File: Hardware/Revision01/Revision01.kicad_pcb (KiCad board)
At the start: 4 copper layers, 100 x 119.8 mm, 63 parts, among them J1 Battery connector, J2 StrainConn, J3 StrainConn, J4 StrainConn, J5 StrainConn, J6 StrainConn, J7 StrainConn, J8 StrainConn, J9 StrainConn, Q3 NMOS, Q4 PMOS, Q6 PMOS, SW2 SW_SPST_LED, U10 NCP1117LPST50T3G, U11 LP5813BDRRR, U2 MRF89XAM9AT-I/RM, U3 NUCLEO-L476RG, U4 ICM-45605

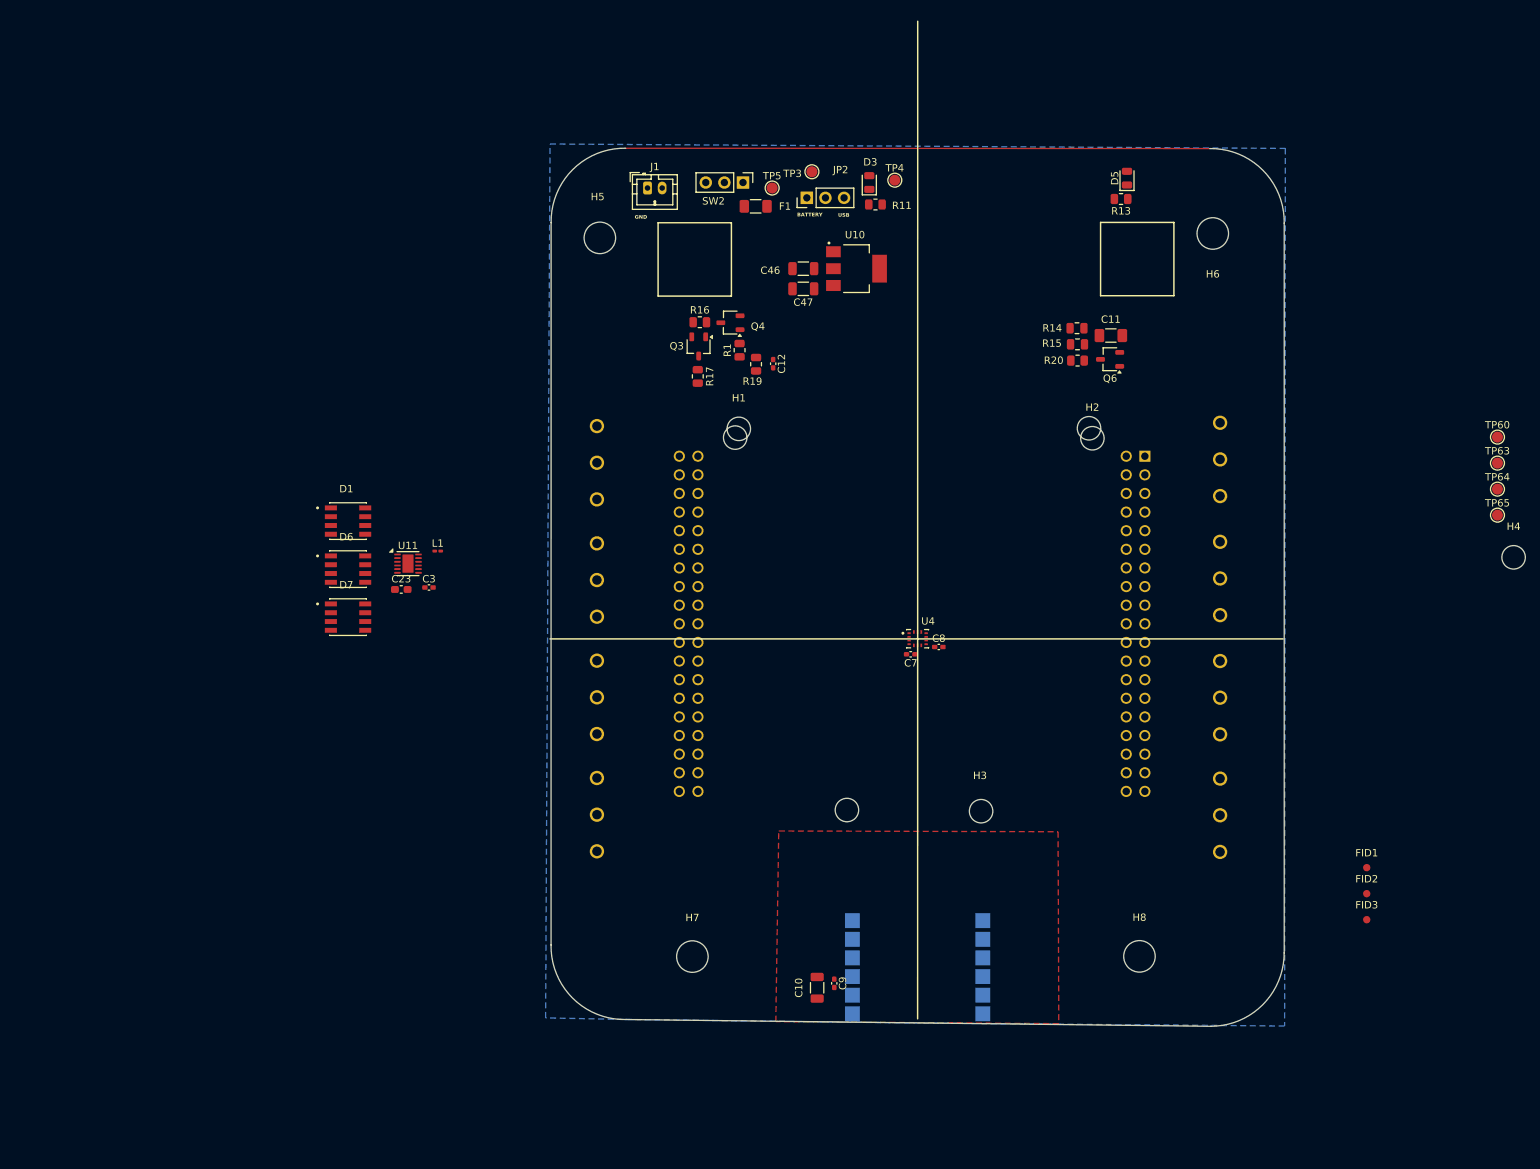
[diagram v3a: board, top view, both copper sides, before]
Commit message: I believe I have finished schematic
-Calculated RC circuit with cutoff at 10KHz for ADC
- Stimulated OP-AMP circuit with strainGauge
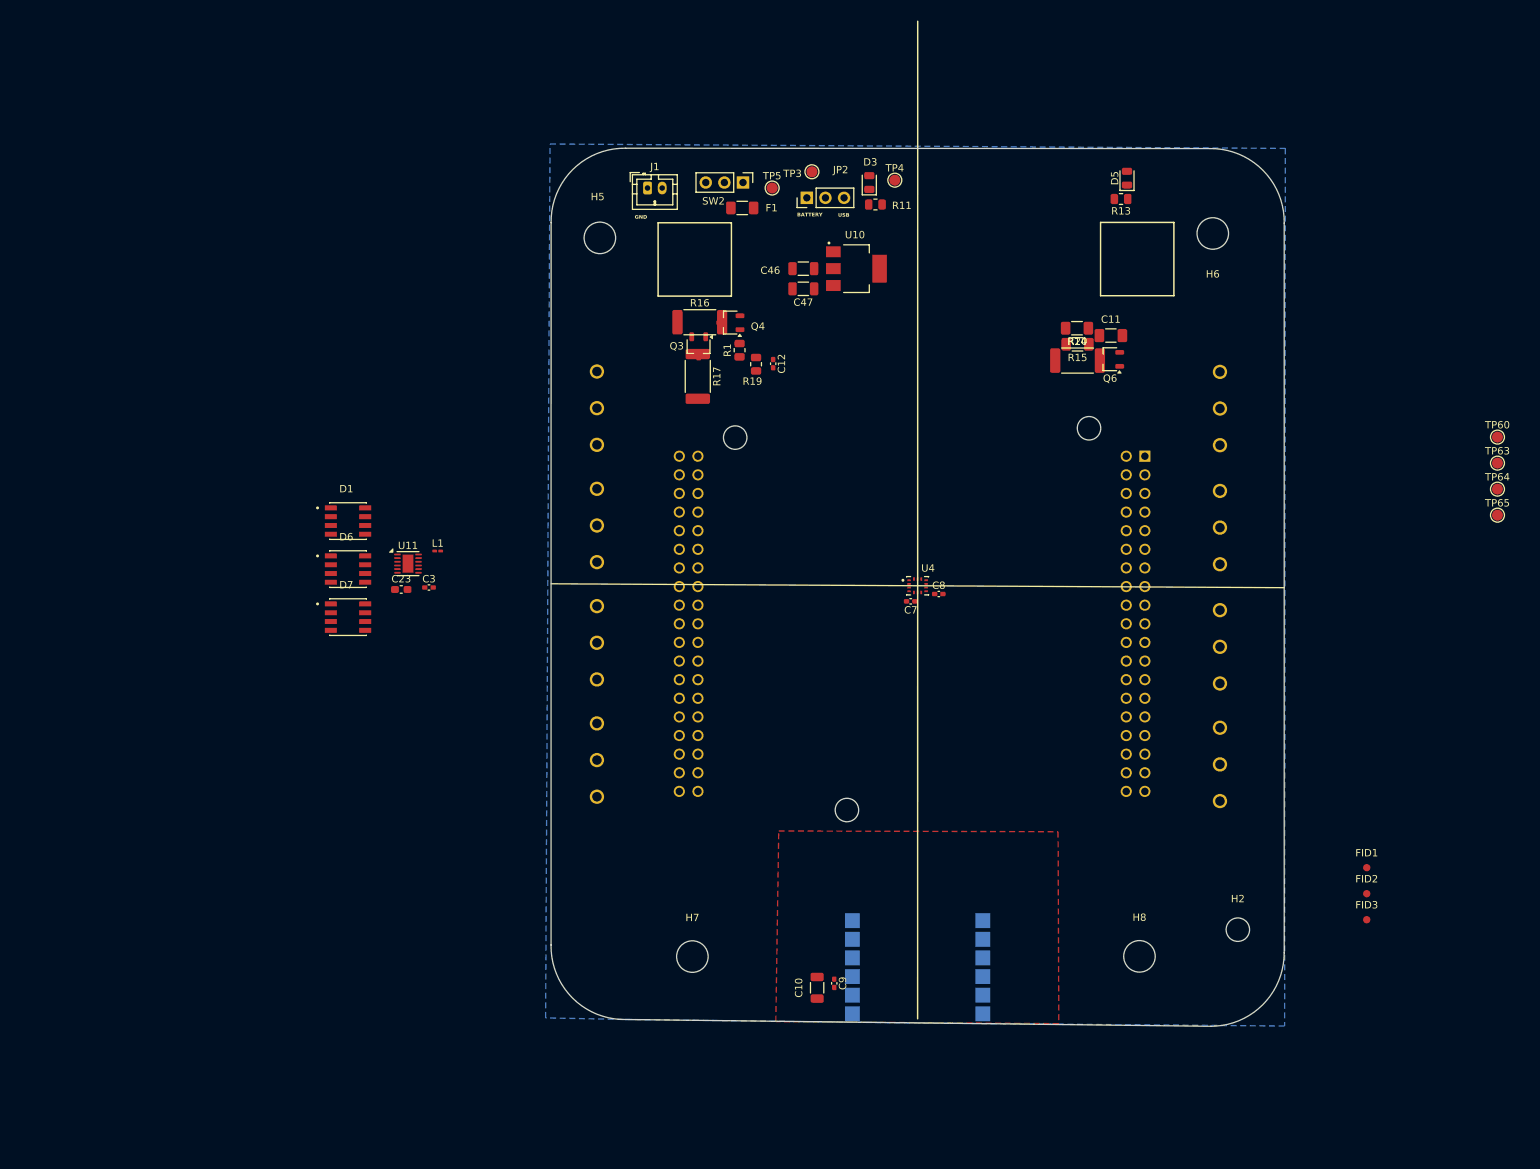
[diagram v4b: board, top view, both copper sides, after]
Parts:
- removed H1, H3, H4: MountingHole, MountingHole:MountingHole_3.2mm_M3
- R14, R15: footprint Capacitor_SMD:C_0805_2012Metric -> Resistor_SMD:R_1206_3216Metric_Pad1.30x1.75mm_HandSolder
- R16, R17, R20: value 10K +-5% -> 10K +-1%; footprint Resistor_SMD:R_0805_2012Metric -> Resistor_SMD:R_2512_6332Metric_Pad1.40x3.35mm_HandSolder
- moved H2 69.9 mm to (204.7, 139.5)
- moved J2 7.44 mm to (117.3, 116.4)
- moved J3 7.44 mm to (117.3, 100.4)
- moved J4 7.44 mm to (117.3, 84.4)
- moved J5 7.44 mm to (117.3, 68.4)
- moved C7 7.22 mm to (160.1, 94.8)
- moved C8 7.22 mm to (163.9, 93.8)
- moved U4 7.22 mm to (161.0, 92.6)
- moved J6 6.94 mm to (202.3, 117.0)
- moved J7 6.94 mm to (202.3, 84.7)
- moved J8 6.94 mm to (202.3, 68.5)
- moved J9 6.94 mm to (202.3, 101.0)
- moved F1 1.84 mm to (137.1, 41.1)
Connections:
- J2 pad 1: /Application/+StrainV -> GND
- J2 pad 3: GND -> /Application/+StrainV
- J3 pad 1: /Application/+StrainV -> GND
- J3 pad 3: GND -> /Application/+StrainV
- J4 pad 1: /Application/+StrainV -> GND
- J4 pad 3: GND -> /Application/+StrainV
- J5 pad 1: /Application/+StrainV -> GND
- J5 pad 3: GND -> /Application/+StrainV
- J6 pad 1: /Application/+StrainV -> GND
- J6 pad 3: GND -> /Application/+StrainV
- J7 pad 1: /Application/+StrainV -> GND
- J7 pad 3: GND -> /Application/+StrainV
- J8 pad 1: /Application/+StrainV -> GND
- J8 pad 3: GND -> /Application/+StrainV
- J9 pad 1: /Application/+StrainV -> GND
- J9 pad 3: GND -> /Application/+StrainV

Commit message: schematic wiring, and LT-SPICE simulations on strain gauge - Added buffer with offset at 1.66V to instrumentation amplifier to ensure -20-20mv range can be read - Added caps to Instrumentation Amplifier circuit - Stimulated straingauge->Amplifier->Adc with all components imported. Verified ADC can read between 0.3-3.0V - Created second draft bom, component cost at around 212$ - Changed many components to Automotive grade - Added breathingCUBE led driver to prototype my own project
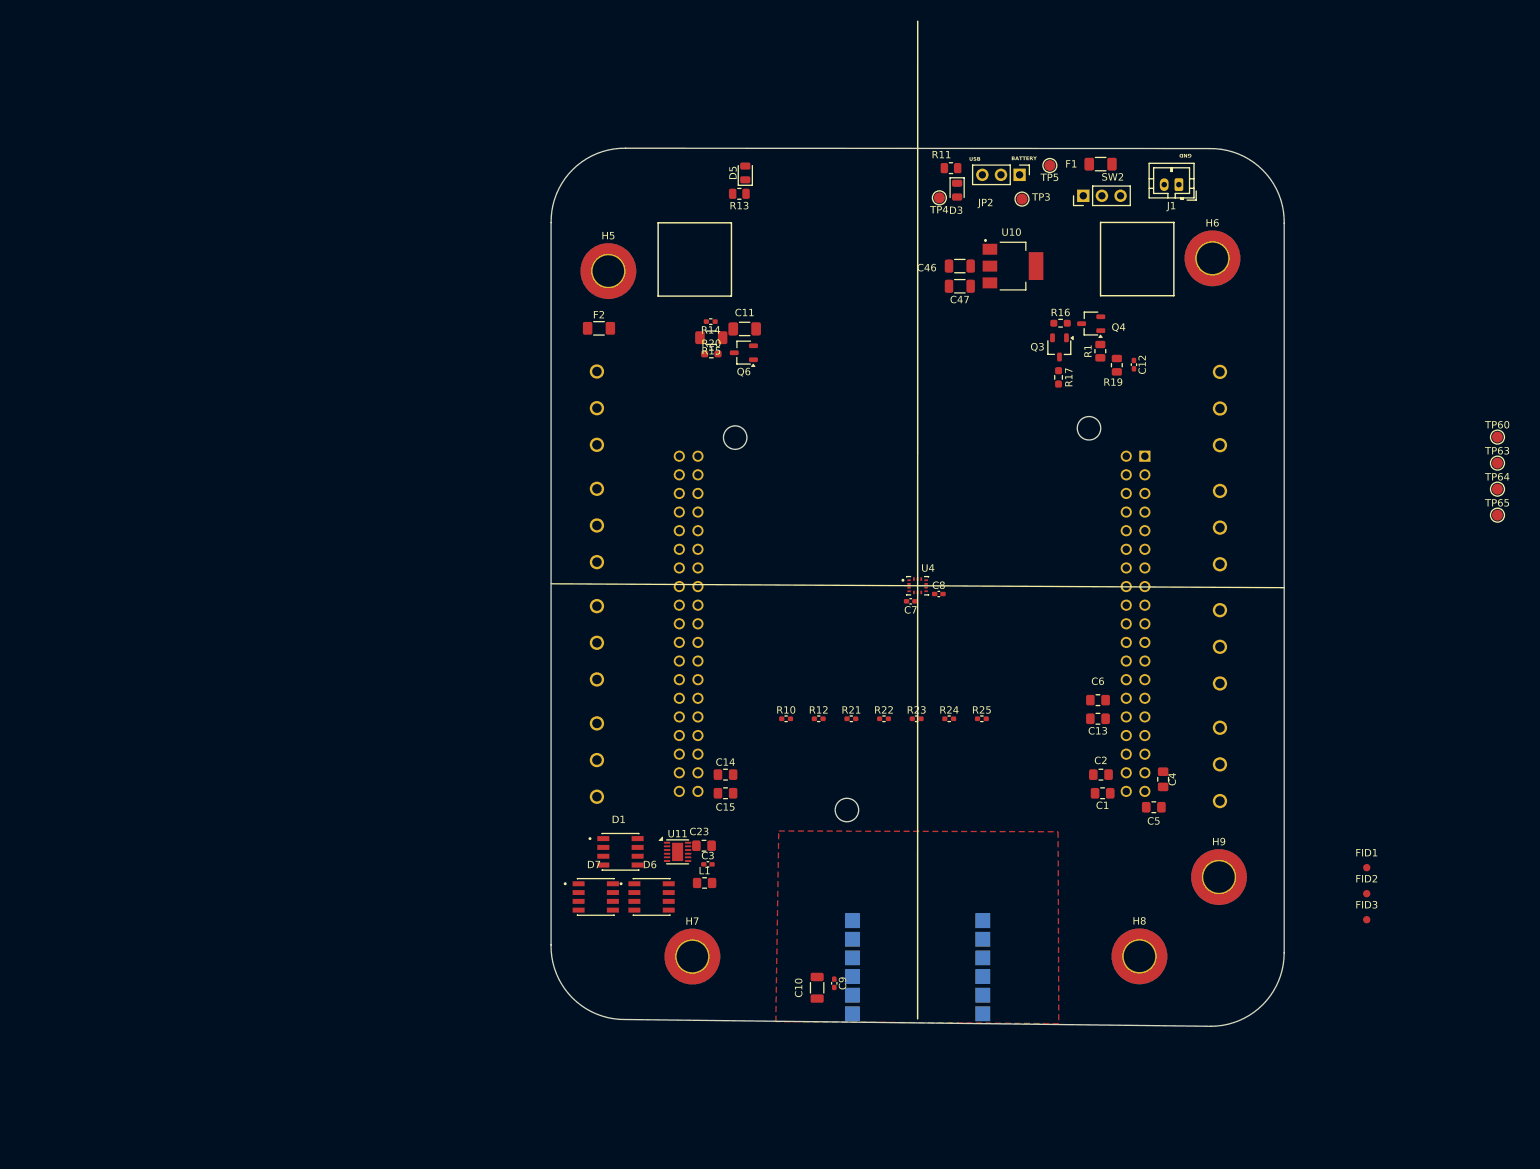
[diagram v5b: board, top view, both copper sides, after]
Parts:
- removed H2: MountingHole, MountingHole:MountingHole_3.2mm_M3
- added C1: 10nF, Capacitor_SMD:C_0805_2012Metric_Pad1.18x1.45mm_HandSolder, F.Cu at (186.3, 120.9)
- added C13: 10nF, Capacitor_SMD:C_0805_2012Metric_Pad1.18x1.45mm_HandSolder, F.Cu at (185.6, 110.8)
- added C14: 10nF, Capacitor_SMD:C_0805_2012Metric_Pad1.18x1.45mm_HandSolder, F.Cu at (134.8, 118.4)
- added C15: 10nF, Capacitor_SMD:C_0805_2012Metric_Pad1.18x1.45mm_HandSolder, F.Cu at (134.8, 120.9)
- added C2: 10nF, Capacitor_SMD:C_0805_2012Metric_Pad1.18x1.45mm_HandSolder, F.Cu at (186.0, 118.4)
- added C4: 10nF, Capacitor_SMD:C_0805_2012Metric_Pad1.18x1.45mm_HandSolder, F.Cu at (194.5, 119.0)
- added C5: 10nF, Capacitor_SMD:C_0805_2012Metric_Pad1.18x1.45mm_HandSolder, F.Cu at (193.2, 122.8)
- added C6: 10nF, Capacitor_SMD:C_0805_2012Metric_Pad1.18x1.45mm_HandSolder, F.Cu at (185.6, 108.2)
- added F2: Polyfuse, Resistor_SMD:R_1206_3216Metric_Pad1.30x1.75mm_HandSolder, F.Cu at (117.6, 57.5)
- added H9: MountingHole_Pad_MP, MountingHole:MountingHole_4.3mm_M4_ISO7380_Pad_TopBottom, F.Cu at (202.1, 132.4)
- added R10: 1.6K +-1%, Resistor_SMD:R_0402_1005Metric_Pad0.72x0.64mm_HandSolder, F.Cu at (143.1, 110.8)
- added R12: 1.6K +-1%, Resistor_SMD:R_0402_1005Metric_Pad0.72x0.64mm_HandSolder, F.Cu at (147.5, 110.8)
- added R21: 1.6K +-1%, Resistor_SMD:R_0402_1005Metric_Pad0.72x0.64mm_HandSolder, F.Cu at (152.0, 110.8)
- added R22: 1.6K +-1%, Resistor_SMD:R_0402_1005Metric_Pad0.72x0.64mm_HandSolder, F.Cu at (156.4, 110.8)
- added R23: 1.6K +-1%, Resistor_SMD:R_0402_1005Metric_Pad0.72x0.64mm_HandSolder, F.Cu at (160.9, 110.8)
- added R24: 1.6K +-1%, Resistor_SMD:R_0402_1005Metric_Pad0.72x0.64mm_HandSolder, F.Cu at (165.3, 110.8)
- added R25: 1.6K +-1%, Resistor_SMD:R_0402_1005Metric_Pad0.72x0.64mm_HandSolder, F.Cu at (169.8, 110.8)
- C23: footprint Capacitor_SMD:C_0603_1608Metric_Pad1.08x0.95mm_HandSolder -> Capacitor_SMD:C_0805_2012Metric_Pad1.18x1.45mm_HandSolder
- H5, H6, H7, H8: value MountingHole -> MountingHole_Pad_MP; footprint MountingHole:MountingHole_4.3mm_M4 -> MountingHole:MountingHole_4.3mm_M4_ISO7380_Pad_TopBottom
- L1: footprint Inductor_SMD:L_0201_0603Metric_Pad0.64x0.40mm_HandSolder -> Inductor_SMD:L_0805_2012Metric_Pad1.15x1.40mm_HandSolder
- R14: value 0K +-1% -> 1.6K +-1%; footprint Resistor_SMD:R_1206_3216Metric_Pad1.30x1.75mm_HandSolder -> Resistor_SMD:R_0402_1005Metric_Pad0.72x0.64mm_HandSolder
- R16, R17, R20: footprint Resistor_SMD:R_2512_6332Metric_Pad1.40x3.35mm_HandSolder -> Resistor_SMD:R_0603_1608Metric_Pad0.98x0.95mm_HandSolder
- moved J1 72.5 mm to (196.7, 37.9), turned to 180 degrees
- moved D6 60.9 mm to (124.7, 135.1)
- moved D1 58.4 mm to (120.5, 128.9)
- moved L1 58.1 mm to (132.0, 133.2)
- moved C23 54.1 mm to (131.9, 128.1)
- moved U11 53.8 mm to (128.3, 128.9)
- moved C3 53.6 mm to (132.4, 130.6)
- moved R13 52.1 mm to (136.7, 39.2)
- moved D5 52.1 mm to (137.5, 36.3)
- moved D7 51.0 mm to (117.1, 135.1)
- moved R20 50.0 mm to (132.9, 61.0)
- moved C11 50.0 mm to (137.4, 57.6)
- moved Q6 50.0 mm to (137.3, 60.9)
- moved R14 50.0 mm to (132.8, 56.6)
- moved R15 50.0 mm to (132.9, 58.8)
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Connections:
- J2 pad 2: /AIN_1 -> /Application/OpAmpOutput1
- J3 pad 2: /AIN_2 -> /Application/OpAmpOutput2
- J4 pad 2: /AIN_3 -> /Application/OpAmpOutput3
- J5 pad 2: /AIN_4 -> /Application/OpAmpOutput4
- J6 pad 2: /AIN_5 -> /Application/OpAmpOutput5
- J7 pad 2: /AIN_7 -> /Application/OpAmpOutput6
- J8 pad 2: /AIN_8 -> /Application/OpAmpOutput7
- J9 pad 2: /AIN_6 -> /Application/OpAmpOutput8
- R14 pad 1: Net-(Q6-S) -> /Application/OpAmpOutput3
- R14 pad 2: +5V -> /AIN_3
- U3 pad CN10_29: unconnected-(U3B-PB5-PadCN10_29) -> /Vref+
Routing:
- added copper zone on In2.Cu, net GND
- removed copper zone on B.Cu, net GND
